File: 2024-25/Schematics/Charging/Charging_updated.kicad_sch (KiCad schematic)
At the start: 32 parts, among them J1 DTM04-12PA-L012, J2 DTM06-12SA, J3 DTM06-12SA, J4 DTM04-12PA-L012, J5 UPCP012ALS2, J6 UPCR012ALS1, J7 UPCR012ALS1, J8 UPCP012ALS2, K1 GV24 1BAX, K2 Relay_DPST-NO, K3 P115 BDA, K4 GV24 1BAX, SW1 84-5330.0020, U2 Relay board, U3 BMS, U4 6.6kW Elcon Charger, U5 RSB, U6 Throttle, U7 Volt_indic, U8 precharge

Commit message: fixed the connectors
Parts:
- added J10: Nema 5-20, symbol Connector:Conn_01x03_Socket
- added J9: J1772, symbol Connector:Conn_01x05_Socket
- U1: value ~ -> IMD
- U6: value Throttle -> Battery Pack
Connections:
- net 12V+: no longer J4.8 (Pin_8)
- net 12V_rect: now also J4.6 (Pin_6); no longer J4.9 (Pin_9)
- net BMS_fault: now also J1.11 (Pin_11)
- net CANH_BMS: now also J1.9 (Pin_9); no longer J2.5 (Pin_5), J3.5 (Pin_5)
- net CANL_BMS: now also J1.10 (Pin_10); no longer J2.4 (Pin_4), J3.4 (Pin_4)
- net CONTROL_PILOT: now also J1.2 (Pin_2), J4.1 (Pin_1), J9.5 (Pin_5)
- net CSS: now also J1.3 (Pin_3), J4.3 (Pin_3); no longer J1.1 (Pin_1), J2.1 (Pin_1), J3.1 (Pin_1), J4.1 (Pin_1)
- net GLV+: now also J1.6 (Pin_6)
- net GLV+_IMD: now also U1.2 (Vs)
- net GNDPWR: now also J4.4 (Pin_4), U1.1 (GND), U1.3 (GND), U1.4 (GND)
- net IMD_fault: now also J1.12 (Pin_12), U1.8 (OKHS)
- net PROX_DET: now also J1.1 (Pin_1), J4.2 (Pin_2), J9.4 (Pin_4)
- net PostAIR+: now also U1.L+ (XLA+)
- net PostAIR-: now also U1.L- (XLA-)
- net SDC1: now also J6.2 (Pin_2); no longer J4.7 (Pin_7)
- net SDC2: now also J4.7 (Pin_7), J6.1 (Pin_1)
- net charge_on: now also J1.4 (Pin_4)
- net at F3.2, F5.2: now also J10.2 (Pin_2), J9.2 (Pin_2)
- net at K2.13, PS1.2 (N): now also J10.3 (Pin_3), J9.3 (Pin_3)
- net at J8.1 (Pin_1): now also J8.2 (Pin_2); no longer J5.1 (Pin_1)
- net at J5.2 (Pin_2): now also J5.1 (Pin_1); no longer J8.2 (Pin_2)
- net at J4.10 (Pin_10): now also U4.7 (CANL)
- net at J4.11 (Pin_11): now also U2. (SW)
- net at J4.12 (Pin_12): now also U2. (SW)
- net at J4.5 (Pin_5): no longer U4.1 (CANH)
- net at U4.8 (CANGND): now also J4.8 (Pin_8); no longer J4.6 (Pin_6)
- net at J3.11 (Pin_11): now also J2.11 (Pin_11)
- net at J3.12 (Pin_12): now also J2.12 (Pin_12)
- net at J2.8 (Pin_8): no longer J3.8 (Pin_8)
- net at J2.9 (Pin_9): no longer J3.9 (Pin_9)
- net at U6. (Therm): no longer U3. (Therm)
- net CANGND_BMS: now reaches J1.8 (Pin_8)
- net at U5. (pre_res-): now also K3.7, K3.8
- net "Chassis" ground: no longer names the net of J2.10 (Pin_10)
- net CANS_BMS: no longer names the net of J2.6 (Pin_6), J3.6 (Pin_6)
- new net: J10.1 (Pin_1), J9.1 (Pin_1), U4. (Output-)
- new net: J2.1 (Pin_1), J3.1 (Pin_1)
- new net: J2.4 (Pin_4), J3.4 (Pin_4)
- new net: J4.9 (Pin_9), U4.1 (CANH)
- new net: U3. (Therm), U6. (Therm) (x4)
- now unconnected: U6. (Therm), U6. (Therm), U6. (Therm)
- no-connect marks 4 -> 2
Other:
- note added: "IMD"
- note added: "lighter orange - 4 awg, shielded"
- note removed: "DASHBOX?"
- note removed: "lighter orange - 1 awg, shielded"
- note removed: "reuse from checkbox connection"
- moved on the sheet: F1, F2, SW1, U2

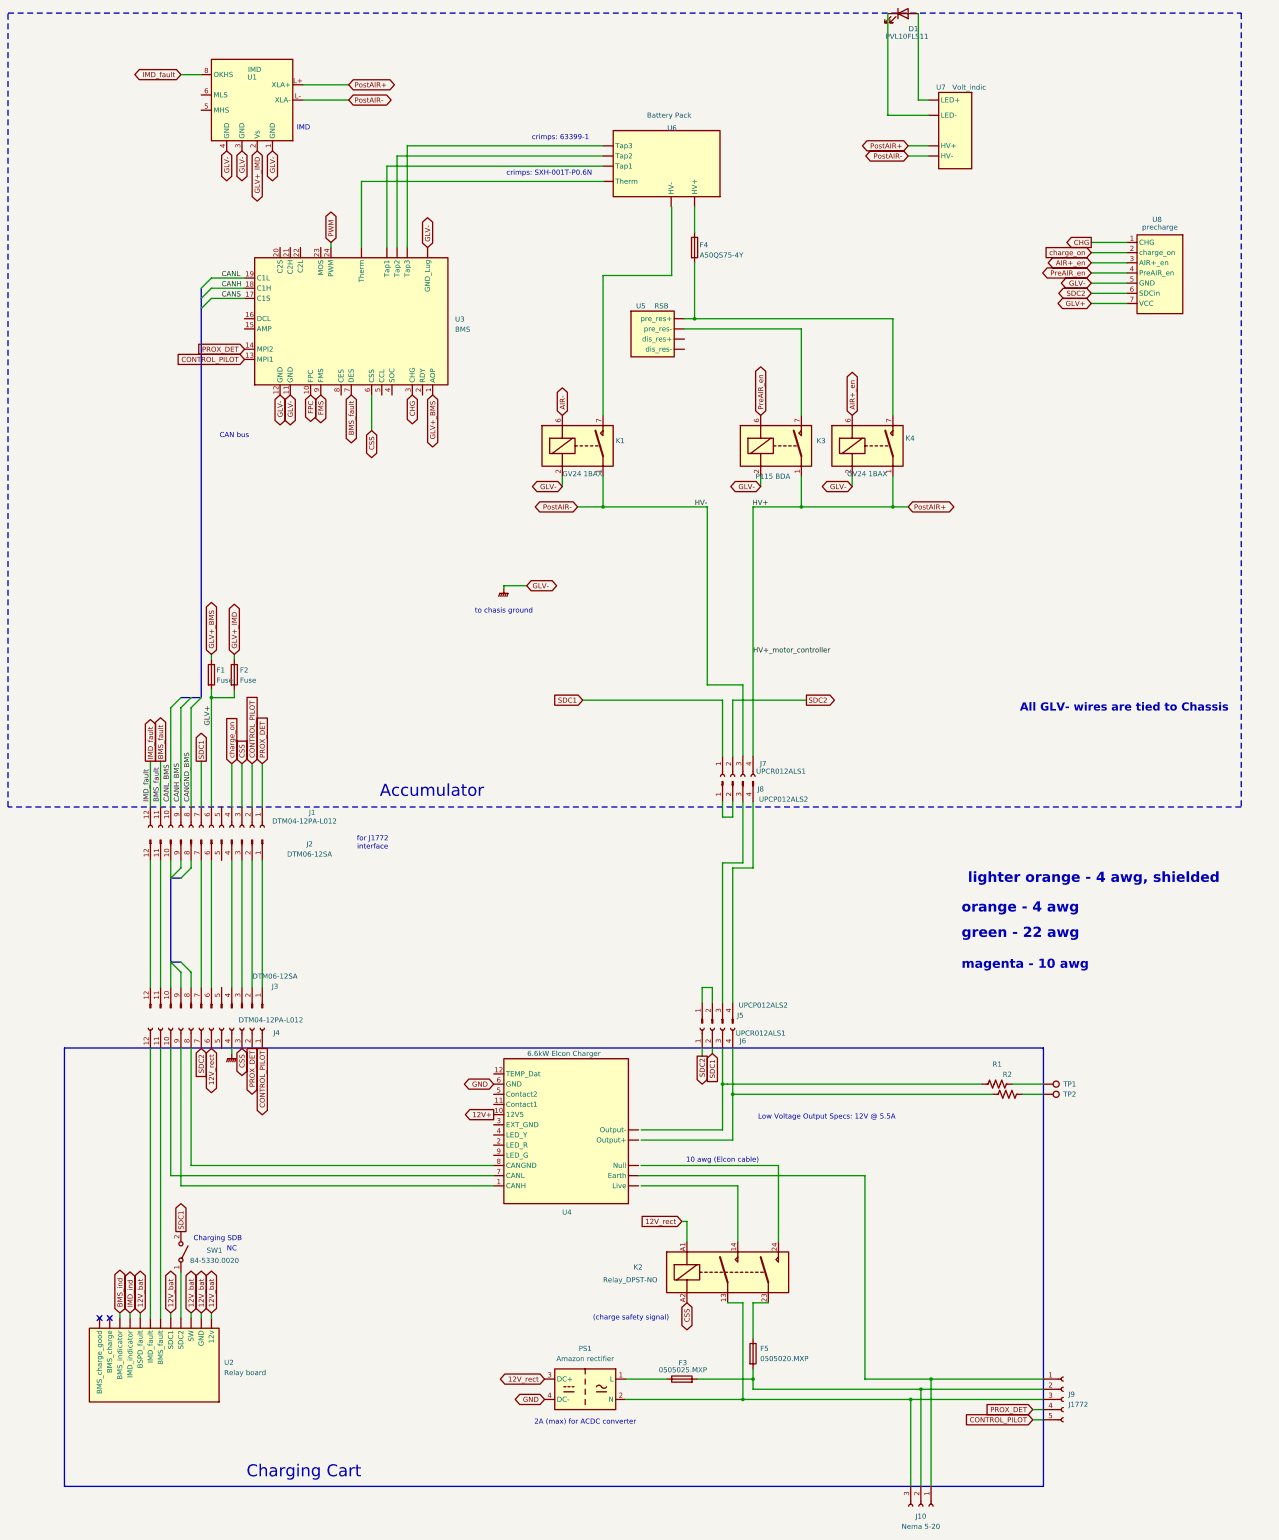
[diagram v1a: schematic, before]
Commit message: fixed some schematics
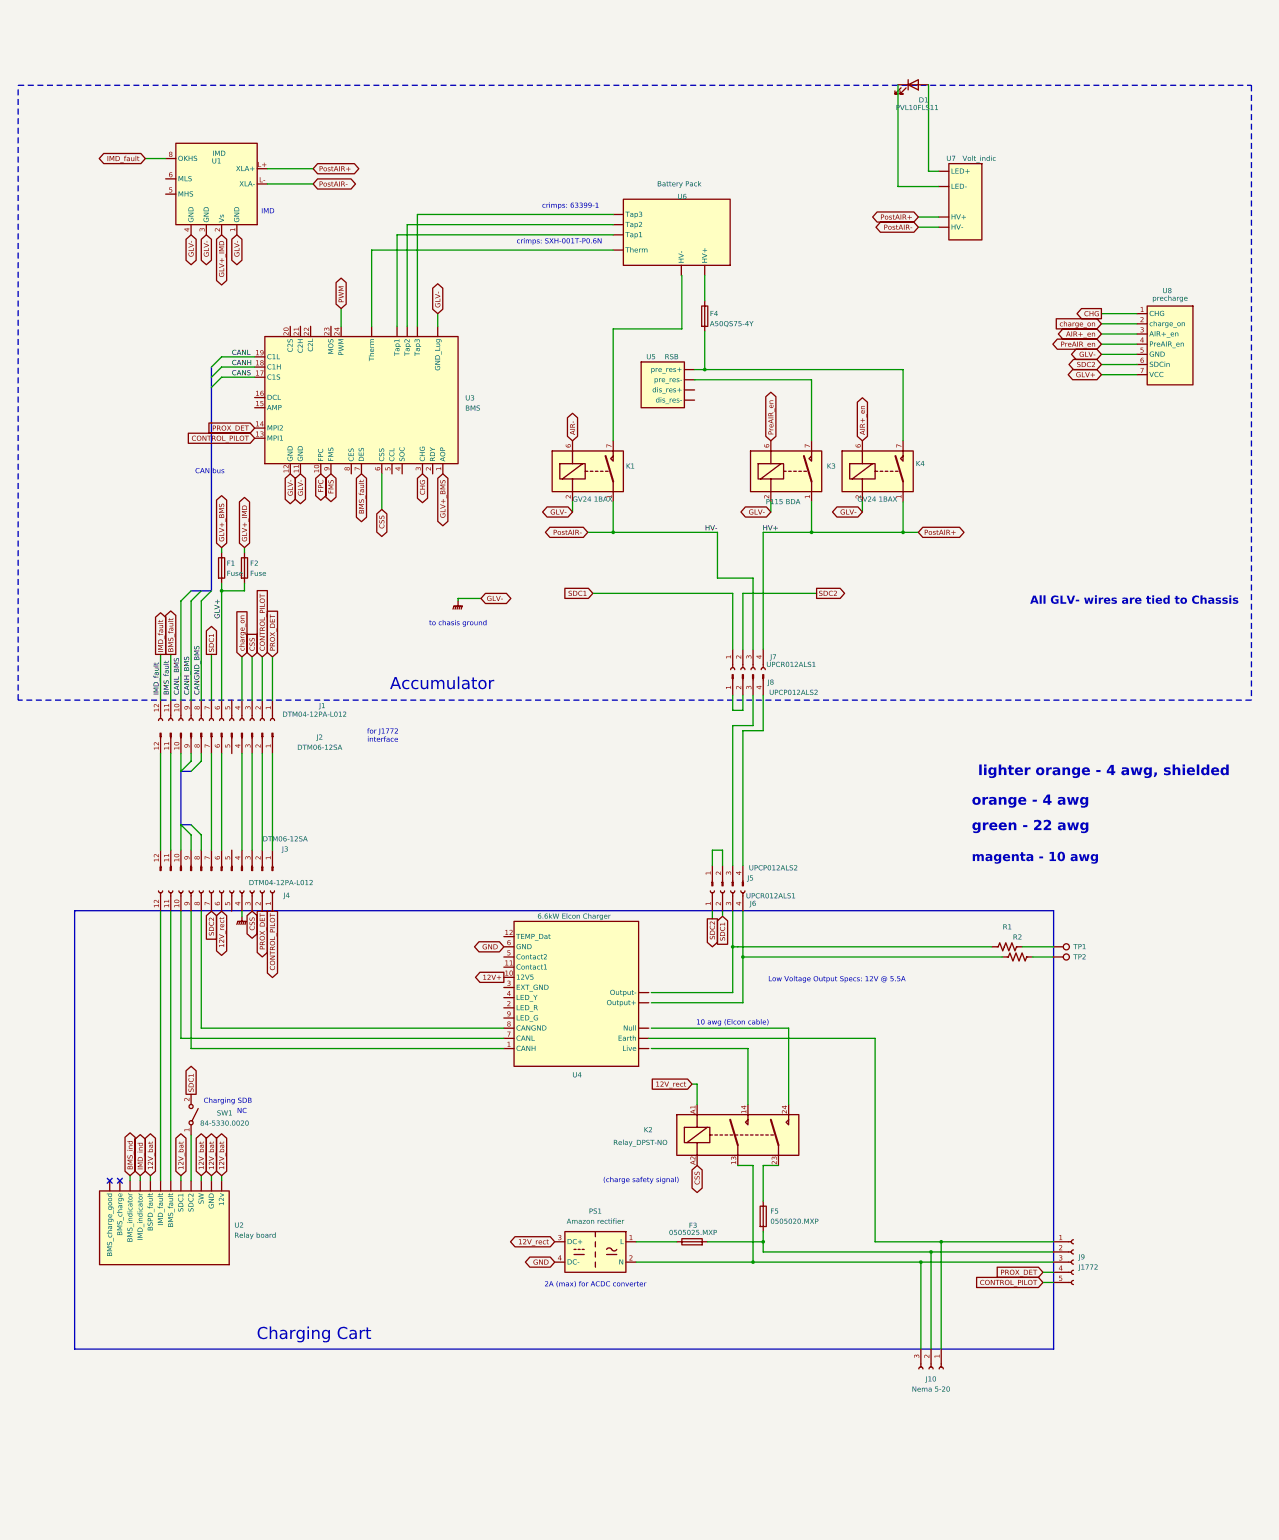
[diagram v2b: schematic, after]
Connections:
- net at U6. (Therm): no longer U3. (Therm)
- net at U5. (pre_res-): now also K3.7, K3.8
- new net: U3. (Therm), U6. (Therm) (x4)
- now unconnected: U6. (Therm), U6. (Therm), U6. (Therm)
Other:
- moved on the sheet: D1, F1, F2, F3, F4, F5, J1, J10, J2, J3, J4, J5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

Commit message: ESF fixes
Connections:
- net at U6. (Therm): no longer U3. (Therm)
- net at U5. (pre_res-): now also K3.7, K3.8
- new net: U3. (Therm), U6. (Therm) (x4)
- now unconnected: U6. (Therm), U6. (Therm), U6. (Therm)
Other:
- note added: "dark red - 4 awg, shielded"
- note removed: "lighter orange - 4 awg, shielded"
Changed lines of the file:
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@@
 			(width 0.5588)
 			(type default)
-			(color 221 133 0 1)
+			(color 72 0 0 1)
 		)
 	)
@@
 			(width 0.5588)
 			(type default)
-			(color 221 133 0 1)
+			(color 72 0 0 1)
 		)
 	)
@@
 			(width 0.5588)
 			(type default)
-			(color 221 133 0 1)
+			(color 72 0 0 1)
 		)
 	)
@@
 			(width 0.5588)
 			(type default)
-			(color 221 133 0 1)
+			(color 72 0 0 1)
 		)
 	)
@@
 			(width 0.5588)
 			(type default)
-			(color 221 133 0 1)
+			(color 72 0 0 1)
 		)
 	)
@@
 			(width 0.5588)
 			(type default)
-			(color 221 133 0 1)
+			(color 72 0 0 1)
 		)
 	)
@@
 		)
 	)
-	(text "lighter orange - 4 awg, shielded"
+	(text "dark red - 4 awg, shielded"
 		(exclude_from_sim no)
-		(at 381 213.995 0)
+		(at 375.158 214.376 0)
 		(effects
 			(font
@@
 				(thickness 0.508)
 				(bold yes)
-				(color 221 133 0 1)
+				(color 72 0 0 1)
 			)
 		)
@@
 	(text "10 awg (Elcon cable)"
 		(exclude_from_sim no)
-		(at 288.29 276.86 0)
+		(at 287.274 279.908 0)
 		(effects
 			(font

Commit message: updated
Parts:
- removed F1: Fuse, symbol Device:Fuse
- removed J7: UPCR012ALS1, symbol Connector:Conn_01x04_Socket
- removed J8: UPCP012ALS2, symbol Connector:Conn_01x04_Pin
- removed U1: IMD, symbol FSAE:IMD
- removed U3: BMS, symbol FSAE:BMS
- removed U5: RSB, symbol Random:RSB
- removed U6: Battery Pack, symbol FSAE:Battery
- removed U7: Volt_indic, symbol Random:Volt_indic
- removed U8: precharge, symbol Random:Precharge
- added F6, F7: Fuse, symbol Device:Fuse
- added J11: UPCR012ALS1, symbol Connector:Conn_01x04_Socket
- added J12: UPCP012ALS1, symbol Connector:Conn_01x04_Pin
- added J13, J7: DTM04-12PA-L012, symbol Connector:Conn_01x12_Socket
- added J14, J8: DTM06-12SA, symbol Connector:Conn_01x12_Pin
- added J20: ??? can't find PN, symbol Connector:Conn_01x04_Socket
- added R4: RCH50S15001JS06, symbol Device:R_US
- added R5: 30k, symbol Device:R
- added R6: 22k, symbol Device:R
- added SW2: reset, symbol Switch:SW_Push
- added U12: IMD, symbol FSAE:IMD
- added U16: Battery Pack, symbol FSAE:Battery
- added U18: BMS, symbol FSAE:BMS
- added U19: DS18B20-PAR, Package_TO_SOT_THT:TO-92_Inline, symbol Sensor_Temperature:DS18B20-PAR
- added U20: RSB, symbol Random:RSB
- added U5: Volt_indic, symbol Random:Volt_indic
- added U6: precharge, symbol Random:Precharge
- F2: value Fuse -> A50QS75-4Y
- F4: value A50QS75-4Y -> Fuse
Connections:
- net AIR- is gone; now on net SDC2: K1.6
- net 12V_rect: now also J4.3 (Pin_3), U2. (BMS_charge_good), SW2.2
- net AIR+_en: now also K4.2, U6.7 (AIR+_en); no longer K4.6
- net BMS_fault: now also J4.11 (Pin_11), U2. (BMS_charge_good), J7.11 (Pin_11), U18.7 (DES); no longer J1.11 (Pin_11)
- net CANGND_BMS: now also J7.10 (Pin_10); no longer J1.8 (Pin_8)
- net CANH: now also U18.18 (C1H)
- net CANH_BMS: now also J7.9 (Pin_9); no longer J1.9 (Pin_9)
- net CANL: now also U18.19 (C1L)
- net CANL_BMS: now also J7.8 (Pin_8); no longer J1.10 (Pin_10)
- net CANS: now also U18.17 (C1S)
- net CHG: now also U18.3 (CHG), U6.3 (CHG)
- net CONTROL_PILOT: now also J4.2 (Pin_2), J13.2 (Pin_2), U18.13 (MPI1); no longer J1.2 (Pin_2), J4.1 (Pin_1)
- net CSS: now also J4.4 (Pin_4); no longer J1.3 (Pin_3), J4.3 (Pin_3)
- net FMS: now also U18.9 (FMS)
- net FPC: now also U18.10 (FPC)
- net GLV+: now also F4.2, F6.2, J7.6 (Pin_6), U6.1 (VCC); no longer F2.2, J1.6 (Pin_6)
- net GLV+_BMS: now also F6.1, U18.1 (AOP)
- net GLV+_IMD: now also F4.1, U12.2 (Vs); no longer F2.1
- net GND: now also R6.2
- net GNDPWR: now also J4.10 (Pin_10), J4.5 (Pin_5), U2. (BMS_charge_good), U4.8 (CANGND), J13.5 (Pin_5), U12.1 (GND), U12.3 (GND), U12.4 (GND), U18. (GND_Lug), U18.11 (GND), U18.12 (GND), U6.2 (GND); no longer J4.4 (Pin_4), K3.2, K4.2
- net IMD_fault: now also J4.12 (Pin_12), U2. (BMS_charge_good), J7.12 (Pin_12), U12.8 (OKHS); no longer J1.12 (Pin_12)
- net PROX_DET: now also J4.1 (Pin_1), J13.1 (Pin_1), U18.14 (MPI2); no longer J1.1 (Pin_1), J4.2 (Pin_2)
- net PostAIR+: now also F7.1, J11.4 (Pin_4), R4.2, U12.L+ (XLA+), U20. (dis_res-), U5. (HV-), U6. (HV-_postair); no longer K3.1, K3.14
- net PostAIR-: now also J11.3 (Pin_3), U12.L- (XLA-), U5. (HV-), U6. (HV-_postair)
- net PreAIR_en: now also K3.2, U6.6 (Pre_en); no longer K3.6
- net SDC1: now also J11.1 (Pin_1), J7.7 (Pin_7); no longer J1.7 (Pin_7)
- net SDC2: now also K3.6, K4.6, J11.2 (Pin_2), R5.1
- net charge_on: now also J13.4 (Pin_4), U6.4 (charge_on); no longer J1.4 (Pin_4)
- net at J5.3 (Pin_3): now also J12.3 (Pin_3)
- net at J5.4 (Pin_4): now also J12.4 (Pin_4)
- net at D1.1 (K): now also U5. (HV-)
- net at D1.2 (A): now also U5. (HV-)
- net at J1.5 (Pin_5): now also J14.5 (Pin_5)
- net at J2.5 (Pin_5): now also J3.5 (Pin_5)
- net at K4.7, K4.8: now also F2.2, K3.7, K3.8; no longer F4.2
- net at U4.7 (CANL): now also J4.8 (Pin_8); no longer J4.10 (Pin_10)
- new net: R5.2, R6.1, U6.5 (SDCin)
- new net: F2.1, U16. (Tap3)
- new net: U16. (Tap3), U18. (GND_Lug) (x4)
- new net: SW2.1, U2. (BMS_charge_good)
- new net: J1.1 (Pin_1), J14.1 (Pin_1)
- new net: J1.10 (Pin_10), J8.10 (Pin_10)
- new net: J1.11 (Pin_11), J8.11 (Pin_11)
- new net: J1.12 (Pin_12), J8.12 (Pin_12)
- new net: J1.2 (Pin_2), J14.2 (Pin_2)
- new net: J1.3 (Pin_3), J14.3 (Pin_3)
- new net: J1.4 (Pin_4), J14.4 (Pin_4)
- new net: J1.6 (Pin_6), J8.6 (Pin_6)
- new net: J1.7 (Pin_7), J8.7 (Pin_7)
- new net: J1.8 (Pin_8), J8.8 (Pin_8)
- new net: J1.9 (Pin_9), J8.9 (Pin_9)
- new net: J12.1 (Pin_1), J12.2 (Pin_2)
- new net Current: J20.1 (Pin_1), J7.5 (Pin_5)
- new net HV+_Emeter: F7.2
- new net HV+_preres: K3.1, K3.14, U20. (dis_res-), U6. (HV-_postair)
- new net HV+_tsmp: R4.1
- new net PC_error: J7.2 (Pin_2), U6.8 (PC_error)
- new net charge_safe: J13.3 (Pin_3), U18.6 (CSS)
- new net temp_GND: J7.4 (Pin_4), U19.1 (GND)
- new net temp_sense: J7.3 (Pin_3), U19.2 (DQ)
- no-connect marks 2 -> 3
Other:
- note added: "Current Sensor"
- note added: "HV+ TSMP resistor & fuse for TSAL HV wire placed here reduced ampacity rule discharge HV+ unfused"
- note removed: "CAN bus"
- note removed: "IMD"
- note removed: "to chasis ground"
- moved on the sheet: J1, J2, J3, J4, SW1, U2

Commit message: Charging updates
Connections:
- net BMS_ind is gone; now on net IMD_fault: U2. (BMS_charge_good)
- net IMD_ind is gone; now on net IMD_fault: U2. (BMS_charge_good)
- net at U16. (Tap3): no longer U18. (GND_Lug)
- new net: U16. (Tap3), U18. (GND_Lug) (x4)
- new net Fault_ind: U2. (BMS_charge_good)
- now unconnected: U16. (Tap3), U16. (Tap3), U16. (Tap3)
- no-connect marks 3 -> 4
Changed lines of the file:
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@@
 		(at 135.255 321.945)
 	)
+	(no_connect
+		(at 137.795 321.945)
+	)
 	(bus_entry
 		(at 165.735 144.78)
@@
 	(wire
 		(pts
-			(xy 137.795 320.675) (xy 137.795 321.945)
-		)
-		(stroke
-			(width 0)
-			(type default)
-		)
-	)
-	(wire
-		(pts
 			(xy 149.225 133.35) (xy 149.225 135.89)
 		)
@@
 		)
 	)
-	(global_label "BMS_ind"
-		(shape bidirectional)
-		(at 137.795 320.675 90)
-		(fields_autoplaced yes)
-		(effects
-			(font
-				(size 1.27 1.27)
-			)
-			(justify left)
-		)
-		(property "Intersheetrefs" "${INTERSHEET_REFS}"
-			(at 137.795 308.7772 90)
-			(effects
-				(font
-					(size 1.27 1.27)
-				)
-				(justify left)
-				(hide yes)
-			)
-		)
-	)
 	(global_label "GLV-"
 		(shape bidirectional)
@@
 		)
 	)
-	(global_label "IMD_ind"
+	(global_label "Fault_ind"
 		(shape bidirectional)
 		(at 140.335 320.675 90)
@@
 		)
 		(property "Intersheetrefs" "${INTERSHEET_REFS}"
-			(at 140.335 309.3819 90)
+			(at 140.335 307.9306 90)
 			(effects
 				(font
